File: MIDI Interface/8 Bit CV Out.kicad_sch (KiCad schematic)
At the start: 6 parts, among them J13 AudioJack2_SwitchT, U4 TL074

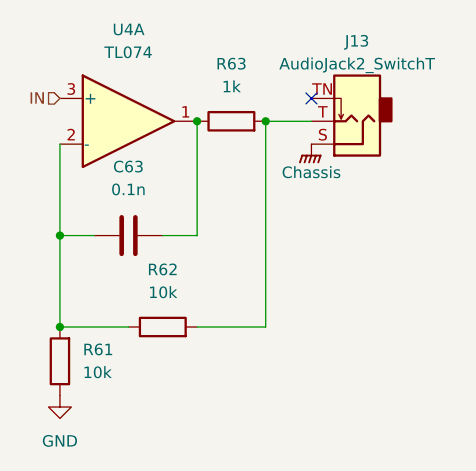
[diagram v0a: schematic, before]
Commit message: Start MIDI interface board
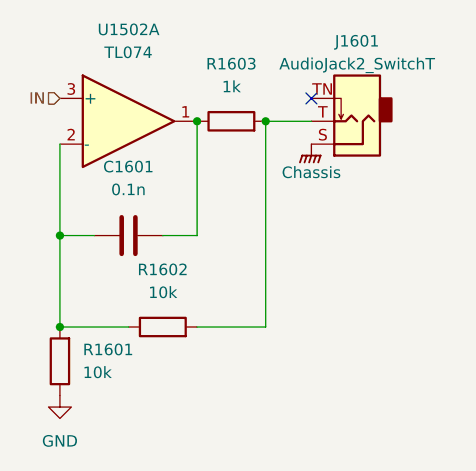
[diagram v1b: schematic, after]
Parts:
- C1601: renamed from C63; footprint (none) -> 0_Capacitor_THT:C_Disc_D5.5mm_W2.5mm_P2.50mm
- J1601: renamed from J13; symbol Connector:AudioJack2_SwitchT -> Connector_Audio:AudioJack2_SwitchT
- R1601: renamed from R61; footprint (none) -> Resistor_THT:R_Axial_DIN0207_L6.3mm_D2.5mm_P7.62mm_Horizontal
- R1602: renamed from R62; footprint (none) -> Resistor_THT:R_Axial_DIN0207_L6.3mm_D2.5mm_P7.62mm_Horizontal
- R1603: renamed from R63; footprint (none) -> Resistor_THT:R_Axial_DIN0207_L6.3mm_D2.5mm_P7.62mm_Horizontal
- U1502: renamed from U4; footprint (none) -> Package_DIP:DIP-14_W7.62mm_Socket

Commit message: New MIDI controller, new envelope generator
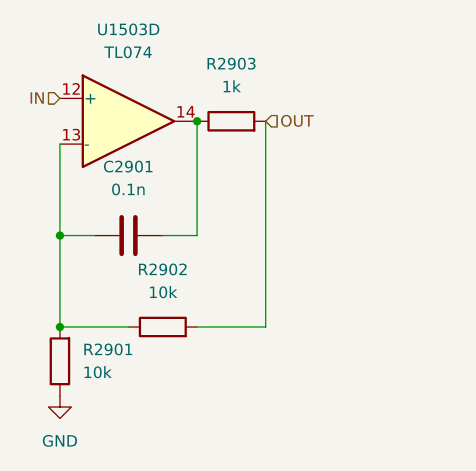
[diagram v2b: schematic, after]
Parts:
- removed J1601: AudioJack2_SwitchT, Connector_Audio:Jack_3.5mm_QingPu_WQP-PJ398SM_Vertical_CircularHoles, symbol Connector_Audio:AudioJack2_SwitchT
- renumbered C1601 to C2901, R1601 to R2901, R1602 to R2902, R1603 to R2903, U1502 to U1503
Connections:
- net IN: now also U1503.12 (+); no longer U1503.3 (+)
- net at C2901.1, R2901.2, R2902.1: now also U1503.13 (-); no longer U1503.2 (-)
- net OUT: now reaches R2902.2, R2903.2
- net at C2901.2, R2903.1: now also U1503.14; no longer U1503.1
- no-connect marks 1 -> 0
